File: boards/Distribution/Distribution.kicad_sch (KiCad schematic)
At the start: 12 parts, among them CN1 B2PS-VH, CN2 Grove, CN3 B3B-ZR, CN4 B3B-ZR, CN5 B3B-ZR, CN6 B3B-ZR, U1 OKL-T/6-W12N

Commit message: modify PCB design
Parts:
- CN2: footprint Connector_JST:JST_PH_B4B-PH-K_1x04_P2.00mm_Vertical -> Grove:GROVE-HW4-2.0
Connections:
- net 5VM: now also CN2.3 (Pin_3); no longer CN2.2 (Pin_2)
- net GND: now also CN2.4 (Pin_4); no longer CN2.1 (Pin_1)
- net SERIAL1: now also CN2.1 (Pin_1); no longer CN2.4 (Pin_4)
- net SERIAL2: now also CN2.2 (Pin_2); no longer CN2.3 (Pin_3)
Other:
- moved on the sheet: CN2
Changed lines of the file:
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@@
 	(symbol
 		(lib_id "Connector_Generic:Conn_01x04")
-		(at 57.15 106.68 180)
+		(at 57.15 104.14 0)
+		(mirror y)
 		(unit 1)
 		(exclude_from_sim no)
@@
 		(dnp no)
 		(property "Reference" "CN2"
-			(at 54.61 106.6801 0)
+			(at 54.61 104.1399 0)
 			(effects
 				(font
@@
 		)
 		(property "Value" "Grove"
-			(at 54.61 104.1401 0)
+			(at 54.61 106.6799 0)
 			(effects
 				(font
@@
 			)
 		)
-		(property "Footprint" "Connector_JST:JST_PH_B4B-PH-K_1x04_P2.00mm_Vertical"
-			(at 57.15 106.68 0)
+		(property "Footprint" "Grove:GROVE-HW4-2.0"
+			(at 57.15 104.14 0)
 			(effects
 				(font
@@
 		)
 		(property "Datasheet" "~"
-			(at 57.15 106.68 0)
+			(at 57.15 104.14 0)
 			(effects
 				(font
@@
 		)
 		(property "Description" "Generic connector, single row, 01x04, script generated (kicad-library-utils/schlib/autogen/connector/)"
-			(at 57.15 106.68 0)
+			(at 57.15 104.14 0)
 			(effects
 				(font
@@
 		)
 		(instances
-			(project ""
+			(project "Distribution"
 				(path "/37f78be0-f9e9-4811-b780-892627006884"
 					(reference "CN2")

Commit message: modify PCB design
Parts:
- U1: value OKL-T/6-W12N -> OKL-T/3-W12N
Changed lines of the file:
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@@
 			)
 		)
-		(property "Value" "OKL-T/6-W12N"
+		(property "Value" "OKL-T/3-W12N"
 			(at 132.842 65.532 0)
 			(effects

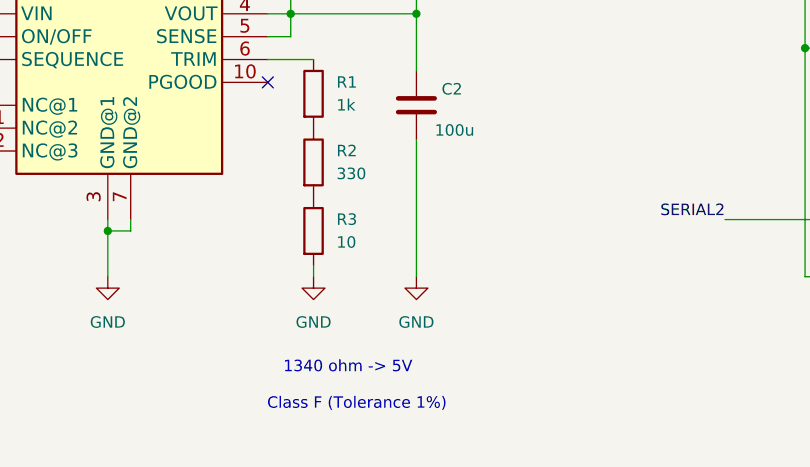
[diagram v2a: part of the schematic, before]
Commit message: fix schematic and BOM
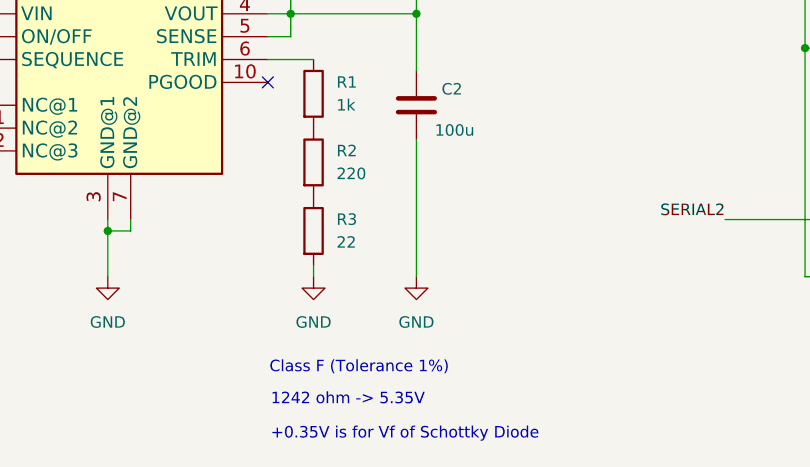
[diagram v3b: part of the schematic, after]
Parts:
- R2: value 330 -> 220
- R3: value 10 -> 22
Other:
- note added: "+0.35V is for Vf of Schottky Diode"
- note added: "1242 ohm -> 5.35V"
- note removed: "1340 ohm -> 5V"
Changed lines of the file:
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@@
 	(title_block
 		(title "Stack-chan Powerd / Distribution Board")
-		(date "2025-06-23")
+		(date "2025-08-11")
 		(rev "1.0")
 	)
@@
 		)
 	)
-	(text "1340 ohm -> 5V"
-		(exclude_from_sim no)
-		(at 158.75 109.22 0)
+	(text "1242 ohm -> 5.35V"
+		(exclude_from_sim no)
+		(at 158.75 112.776 0)
 		(effects
 			(font
@@
 		)
 	)
+	(text "+0.35V is for Vf of Schottky Diode"
+		(exclude_from_sim no)
+		(at 165.1 116.586 0)
+		(effects
+			(font
+				(size 1.27 1.27)
+			)
+		)
+	)
 	(text "(JST ZH Top Type)"
 		(exclude_from_sim no)
@@
 	(text "Class F (Tolerance 1%)"
 		(exclude_from_sim no)
-		(at 159.766 113.284 0)
+		(at 160.02 109.22 0)
 		(effects
 			(font
@@
 			)
 		)
-		(property "Value" "330"
+		(property "Value" "220"
 			(at 157.48 87.6299 0)
 			(effects
@@
 			)
 		)
-		(property "Value" "10"
+		(property "Value" "22"
 			(at 157.48 95.2499 0)
 			(effects
